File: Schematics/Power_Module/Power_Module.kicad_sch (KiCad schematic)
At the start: 0 parts

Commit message: major layout progress, still need to place MCU
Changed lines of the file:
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@@
 		(comment 4 "GRID = 0.635mm")
 	)
-	(text_box "TODO\n - Add GSE_SENSE and 24V_CURR_SENSE\n - Review COMP C and R\n - Review 24V current sensing"
+	(text_box "TODO\n - Add GSE_SENSE and 24V_CURR_SENSE\n - Review COMP C and R\n - Review 24V current sensing\n - find a few small decen size buck caps (https://www.digikey.ca/en/products/filter/aluminum-electrolytic-capacitors/w%C3%BCrth-elektronik/58?s=N4IgjCBcoCwGxVAYygMwIYBsDOBTANCAPZQDa4AzABwAMVIhYATEzRIzdQOwgC6hABwAuUEAGUhAJwCWAOwDmIAL6E4ATkQgUkDDgLEyIGDTUVTfQSMjipcxSpCsuG6FrRY8hEpHJgaAAgA1BnA4IJCKAFZwwiZo4MJIgOD%2BEGFRAFVZaSEAeVQAWVx0bABXSVxlQgBaCFdtXU8QADdZKClS-W9yLgomCzSrGxkFZSUlIA)\n - double check the voltage devider resisters can take the current"
 		(exclude_from_sim no)
 		(at 113.03 115.0112 0)

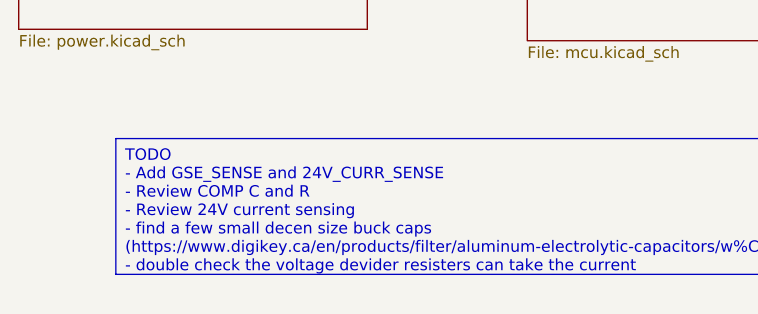
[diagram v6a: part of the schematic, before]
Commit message: continueing layout, confirmed all devices will fix  - need to add bulk rail caps  - fixed issue in oring logic
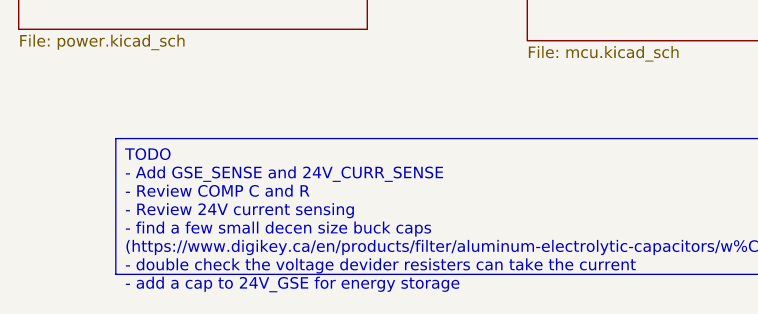
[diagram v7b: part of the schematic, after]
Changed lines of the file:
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@@
 		(comment 4 "GRID = 0.635mm")
 	)
-	(text_box "TODO\n - Add GSE_SENSE and 24V_CURR_SENSE\n - Review COMP C and R\n - Review 24V current sensing\n - find a few small decen size buck caps (https://www.digikey.ca/en/products/filter/aluminum-electrolytic-capacitors/w%C3%BCrth-elektronik/58?s=N4IgjCBcoCwGxVAYygMwIYBsDOBTANCAPZQDa4AzABwAMVIhYATEzRIzdQOwgC6hABwAuUEAGUhAJwCWAOwDmIAL6E4ATkQgUkDDgLEyIGDTUVTfQSMjipcxSpCsuG6FrRY8hEpHJgaAAgA1BnA4IJCKAFZwwiZo4MJIgOD%2BEGFRAFVZaSEAeVQAWVx0bABXSVxlQgBaCFdtXU8QADdZKClS-W9yLgomCzSrGxkFZSUlIA)\n - double check the voltage devider resisters can take the current"
+	(text_box "TODO\n - Add GSE_SENSE and 24V_CURR_SENSE\n - Review COMP C and R\n - Review 24V current sensing\n - find a few small decen size buck caps (https://www.digikey.ca/en/products/filter/aluminum-electrolytic-capacitors/w%C3%BCrth-elektronik/58?s=N4IgjCBcoCwGxVAYygMwIYBsDOBTANCAPZQDa4AzABwAMVIhYATEzRIzdQOwgC6hABwAuUEAGUhAJwCWAOwDmIAL6E4ATkQgUkDDgLEyIGDTUVTfQSMjipcxSpCsuG6FrRY8hEpHJgaAAgA1BnA4IJCKAFZwwiZo4MJIgOD%2BEGFRAFVZaSEAeVQAWVx0bABXSVxlQgBaCFdtXU8QADdZKClS-W9yLgomCzSrGxkFZSUlIA)\n - double check the voltage devider resisters can take the current\n - add a cap to 24V_GSE for energy storage"
 		(exclude_from_sim no)
 		(at 113.03 115.0112 0)

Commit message: confirm layout, confirm everything fits
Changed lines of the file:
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@@
 		(comment 4 "GRID = 0.635mm")
 	)
-	(text_box "TODO\n - Add GSE_SENSE and 24V_CURR_SENSE\n - Review COMP C and R\n - Review 24V current sensing\n - find a few small decen size buck caps (https://www.digikey.ca/en/products/filter/aluminum-electrolytic-capacitors/w%C3%BCrth-elektronik/58?s=N4IgjCBcoCwGxVAYygMwIYBsDOBTANCAPZQDa4AzABwAMVIhYATEzRIzdQOwgC6hABwAuUEAGUhAJwCWAOwDmIAL6E4ATkQgUkDDgLEyIGDTUVTfQSMjipcxSpCsuG6FrRY8hEpHJgaAAgA1BnA4IJCKAFZwwiZo4MJIgOD%2BEGFRAFVZaSEAeVQAWVx0bABXSVxlQgBaCFdtXU8QADdZKClS-W9yLgomCzSrGxkFZSUlIA)\n - double check the voltage devider resisters can take the current\n - add a cap to 24V_GSE for energy storage"
+	(text_box "TODO\n - Add GSE_SENSE and 24V_CURR_SENSE\n - Review COMP C and R\n - Review 24V current sensing\n - find a few small decen size buck caps (https://www.digikey.ca/en/products/filter/aluminum-electrolytic-capacitors/w%C3%BCrth-elektronik/58?s=N4IgjCBcoCwGxVAYygMwIYBsDOBTANCAPZQDa4AzABwAMVIhYATEzRIzdQOwgC6hABwAuUEAGUhAJwCWAOwDmIAL6E4ATkQgUkDDgLEyIGDTUVTfQSMjipcxSpCsuG6FrRY8hEpHJgaAAgA1BnA4IJCKAFZwwiZo4MJIgOD%2BEGFRAFVZaSEAeVQAWVx0bABXSVxlQgBaCFdtXU8QADdZKClS-W9yLgomCzSrGxkFZSUlIA)\n - double check the voltage devider resisters can take the current\n - add a cap to 24V_GSE for energy storage\n - review LCSC, noticed one was out of stock"
 		(exclude_from_sim no)
 		(at 113.03 115.0112 0)
